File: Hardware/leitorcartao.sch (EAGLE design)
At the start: 161 parts, among them IC1 TL084, IC2 TL084, Q1 DMN3404, Q4 BC847ALT1SMD, Q5 BC847ALT1SMD, Q6 BC847ALT1SMD, Q7 BC847ALT1SMD, Q8 MMBT4403, Q9 MMBT4401, U1 SAMD20E14A-AUT, U3 TLV1117-50CDCYR, U4 MFRC52202HN1, U5 LP2985-33DBVR, X1 MIFARE, X3 ANTENA, Y1 27.12MHz

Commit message: Mais progressos em isolar todos os componentes na camada superior.
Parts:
- removed SJ?1: SOLDERBRIDGE, RFiD:SOLDERBRIDGE
- added JP1: (no value), pinhead:PINHD-2X3
- Y1: device RFiD:CRISTALSMALL(3.2X2.5MM) -> ACESSO:CRISTALSMALL(3.2X2.5MM); CUSTOMER_PN XTAL/2712MHZ/3x2 -> (none)
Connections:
- removed net N$77: R44.2, SG1.+, SJ?1.2
- net +12V: now also R44.2, SG1.+; no longer SJ?1.1
- net +3V3: no longer SJ?1.3
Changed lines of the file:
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@@
 <part name="GND42" library="supply1" deviceset="GND" device=""/>
 <part name="GND43" library="supply1" deviceset="GND" device=""/>
-<part name="Y1" library="RFiD" deviceset="CRISTAL" device="SMALL(3.2X2.5MM)" value="27.12MHz">
-<attribute name="CUSTOMER_PN" value="XTAL/2712MHZ/3x2"/>
-</part>
 <part name="C5" library="RFiD" deviceset="C-US" device="C0402" value="18p">
 <attribute name="CUSTOMER_PN" value="C/18p/16V/C04"/>
@@
 <attribute name="CUSTOMER_PN" value="R/1k/5%/04"/>
 </part>
-<part name="+3V16" library="supply1" deviceset="+3V3" device=""/>
 <part name="D5" library="RFiD" deviceset="BAT54S" device="">
 <attribute name="CUSTOMER_PN" value="D/BAT54S"/>
@@
 <part name="P+10" library="supply1" deviceset="V+" device=""/>
 <part name="P+12" library="supply1" deviceset="+12V" device=""/>
-<part name="SJ?1" library="RFiD" deviceset="SOLDERBRIDGE" device=""/>
 <part name="P+16" library="supply1" deviceset="+12V" device=""/>
 <part name="C43" library="RFiD" deviceset="C-US" device="C0402" value="0.1u"/>
@@
 <part name="C60" library="RFiD" deviceset="C-US" device="C0402" value="0.1u"/>
 <part name="GND30" library="supply1" deviceset="GND" device=""/>
+<part name="JP1" library="pinhead" deviceset="PINHD-2X3" device=""/>
+<part name="Y1" library="ACESSO" deviceset="CRISTAL" device="SMALL(3.2X2.5MM)" value="27.12MHz"/>
 </parts>
 <sheets>
@@
 <instance part="X3" gate="-1" x="45.72" y="134.62"/>
 <instance part="X3" gate="-2" x="45.72" y="132.08"/>
+<instance part="JP1" gate="A" x="-17.78" y="55.88"/>
 </instances>
 <busses>
@@
 <instance part="GND42" gate="1" x="200.66" y="152.4"/>
 <instance part="GND43" gate="1" x="213.36" y="152.4"/>
-<instance part="Y1" gate="G$1" x="43.18" y="137.16" smashed="yes" rot="R90">
-<attribute name="NAME" x="45.72" y="140.716" size="1.778" layer="95"/>
-<attribute name="VALUE" x="45.212" y="131.318" size="1.778" layer="96"/>
-<attribute name="CUSTOMER_PN" x="43.18" y="137.16" size="1.778" layer="96" display="off"/>
-</instance>
 <instance part="C5" gate="G$1" x="38.1" y="149.86" smashed="yes" rot="R270">
 <attribute name="NAME" x="33.528" y="153.035" size="1.778" layer="95"/>
@@
 <instance part="X1" gate="-1" x="243.84" y="66.04"/>
 <instance part="X1" gate="-2" x="243.84" y="63.5"/>
+<instance part="Y1" gate="G$1" x="43.18" y="137.16" smashed="yes" rot="R90">
+<attribute name="NAME" x="41.656" y="141.732" size="1.778" layer="95" rot="R180"/>
+<attribute name="VALUE" x="56.388" y="133.604" size="1.778" layer="96" rot="R180"/>
+</instance>
 </instances>
 <busses>
@@
 </segment>
 <segment>
-<pinref part="Y1" gate="G$1" pin="GND@2"/>
 <pinref part="GND14" gate="1" pin="GND"/>
 <wire x1="38.1" y1="137.16" x2="30.48" y2="137.16" width="0.1524" layer="91"/>
@@
 <wire x1="33.02" y1="124.46" x2="30.48" y2="124.46" width="0.1524" layer="91"/>
 <wire x1="30.48" y1="124.46" x2="30.48" y2="137.16" width="0.1524" layer="91"/>
+<pinref part="Y1" gate="G$1" pin="GND@2"/>
 </segment>
 <segment>
 <pinref part="GND13" gate="1" pin="GND"/>
-<pinref part="Y1" gate="G$1" pin="GND@1"/>
 <wire x1="50.8" y1="137.16" x2="48.26" y2="137.16" width="0.1524" layer="91"/>
+<pinref part="Y1" gate="G$1" pin="GND@1"/>
 </segment>
 <segment>
@@
 <wire x1="66.04" y1="139.7" x2="60.96" y2="139.7" width="0.1524" layer="91"/>
 <wire x1="60.96" y1="139.7" x2="60.96" y2="144.78" width="0.1524" layer="91"/>
-<pinref part="Y1" gate="G$1" pin="2"/>
 <wire x1="60.96" y1="144.78" x2="43.18" y2="144.78" width="0.1524" layer="91"/>
 <wire x1="43.18" y1="144.78" x2="43.18" y2="139.7" width="0.1524" layer="91"/>
@@
 <pinref part="C5" gate="G$1" pin="1"/>
 <wire x1="43.18" y1="149.86" x2="40.64" y2="149.86" width="0.1524" layer="91"/>
+<pinref part="Y1" gate="G$1" pin="2"/>
 </segment>
 </net>
@@
 <wire x1="66.04" y1="134.62" x2="60.96" y2="134.62" width="0.1524" layer="91"/>
 <wire x1="60.96" y1="134.62" x2="60.96" y2="129.54" width="0.1524" layer="91"/>
-<pinref part="Y1" gate="G$1" pin="1"/>
 <wire x1="60.96" y1="129.54" x2="43.18" y2="129.54" width="0.1524" layer="91"/>
 <wire x1="43.18" y1="129.54" x2="43.18" y2="134.62" width="0.1524" layer="91"/>
@@
 <wire x1="43.18" y1="124.46" x2="43.18" y2="129.54" width="0.1524" layer="91"/>
 <junction x="43.18" y="129.54"/>
+<pinref part="Y1" gate="G$1" pin="1"/>
 </segment>
 </net>
@@
 <attribute name="CUSTOMER_PN" x="35.56" y="139.7" size="1.778" layer="96" display="off"/>
 </instance>
-<instance part="+3V16" gate="G$1" x="25.4" y="162.56"/>
 <instance part="D5" gate="G$1" x="208.28" y="157.48" rot="R180">
 <attribute name="CUSTOMER_PN" x="208.28" y="157.48" size="1.778" layer="96" display="off"/>
@@
 <instance part="+3V18" gate="G$1" x="198.12" y="162.56"/>
 <instance part="+3V19" gate="G$1" x="198.12" y="132.08"/>
-<instance part="SJ?1" gate="G$1" x="35.56" y="154.94" rot="R180"/>
-<instance part="P+16" gate="1" x="48.26" y="162.56"/>
+<instance part="P+16" gate="1" x="35.56" y="154.94"/>
 <instance part="LED2" gate="G$1" x="109.22" y="124.46"/>
 <instance part="GND19" gate="1" x="106.68" y="114.3"/>
@@
 <wire x1="198.12" y1="127" x2="198.12" y2="129.54" width="0.1524" layer="91"/>
 </segment>
-<segment>
-<pinref part="+3V16" gate="G$1" pin="+3V3"/>
-<pinref part="SJ?1" gate="G$1" pin="3"/>
-<wire x1="25.4" y1="160.02" x2="25.4" y2="154.94" width="0.1524" layer="91"/>
-<wire x1="25.4" y1="154.94" x2="30.48" y2="154.94" width="0.1524" layer="91"/>
-</segment>
 </net>
 <net name="N$54" class="0">
@@
 </segment>
 </net>
-<net name="+12V" class="0">
-<segment>
-<pinref part="SJ?1" gate="G$1" pin="1"/>
-<pinref part="P+16" gate="1" pin="+12V"/>
-<wire x1="40.64" y1="154.94" x2="48.26" y2="154.94" width="0.1524" layer="91"/>
-<wire x1="48.26" y1="154.94" x2="48.26" y2="160.02" width="0.1524" layer="91"/>
-</segment>
-</net>
 <net name="N$18" class="0">
 <segment>
@@
 </segment>
 </net>
-<net name="N$77" class="0">
-<segment>
-<pinref part="R44" gate="G$1" pin="2"/>
-<wire x1="35.56" y1="144.78" x2="35.56" y2="147.32" width="0.1524" layer="91"/>
-<pinref part="SG1" gate="1" pin="+"/>
-<wire x1="45.72" y1="144.78" x2="45.72" y2="147.32" width="0.1524" layer="91"/>
-<wire x1="45.72" y1="147.32" x2="35.56" y2="147.32" width="0.1524" layer="91"/>
-<pinref part="SJ?1" gate="G$1" pin="2"/>
-<wire x1="35.56" y1="147.32" x2="35.56" y2="152.4" width="0.1524" layer="91"/>
-<junction x="35.56" y="147.32"/>
-</segment>
-</net>
 <net name="N$52" class="0">
 <segment>
@@
 </segment>
 </net>
+<net name="+12V" class="0">
+<segment>
+<pinref part="R44" gate="G$1" pin="2"/>
+<wire x1="35.56" y1="144.78" x2="35.56" y2="147.32" width="0.1524" layer="91"/>
+<pinref part="SG1" gate="1" pin="+"/>
+<wire x1="45.72" y1="144.78" x2="45.72" y2="147.32" width="0.1524" layer="91"/>
+<wire x1="45.72" y1="147.32" x2="35.56" y2="147.32" width="0.1524" layer="91"/>
+<wire x1="35.56" y1="147.32" x2="35.56" y2="152.4" width="0.1524" layer="91"/>
+<junction x="35.56" y="147.32"/>
+<pinref part="P+16" gate="1" pin="+12V"/>
+</segment>
+</net>

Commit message: Última versão do posicionamento.
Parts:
- removed JP1: (no value), pinhead:PINHD-2X3
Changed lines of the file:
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@@
 <part name="C60" library="RFiD" deviceset="C-US" device="C0402" value="0.1u"/>
 <part name="GND30" library="supply1" deviceset="GND" device=""/>
-<part name="JP1" library="pinhead" deviceset="PINHD-2X3" device=""/>
 <part name="Y1" library="ACESSO" deviceset="CRISTAL" device="SMALL(3.2X2.5MM)" value="27.12MHz"/>
 </parts>
@@
 <instance part="X3" gate="-1" x="45.72" y="134.62"/>
 <instance part="X3" gate="-2" x="45.72" y="132.08"/>
-<instance part="JP1" gate="A" x="-17.78" y="55.88"/>
 </instances>
 <busses>

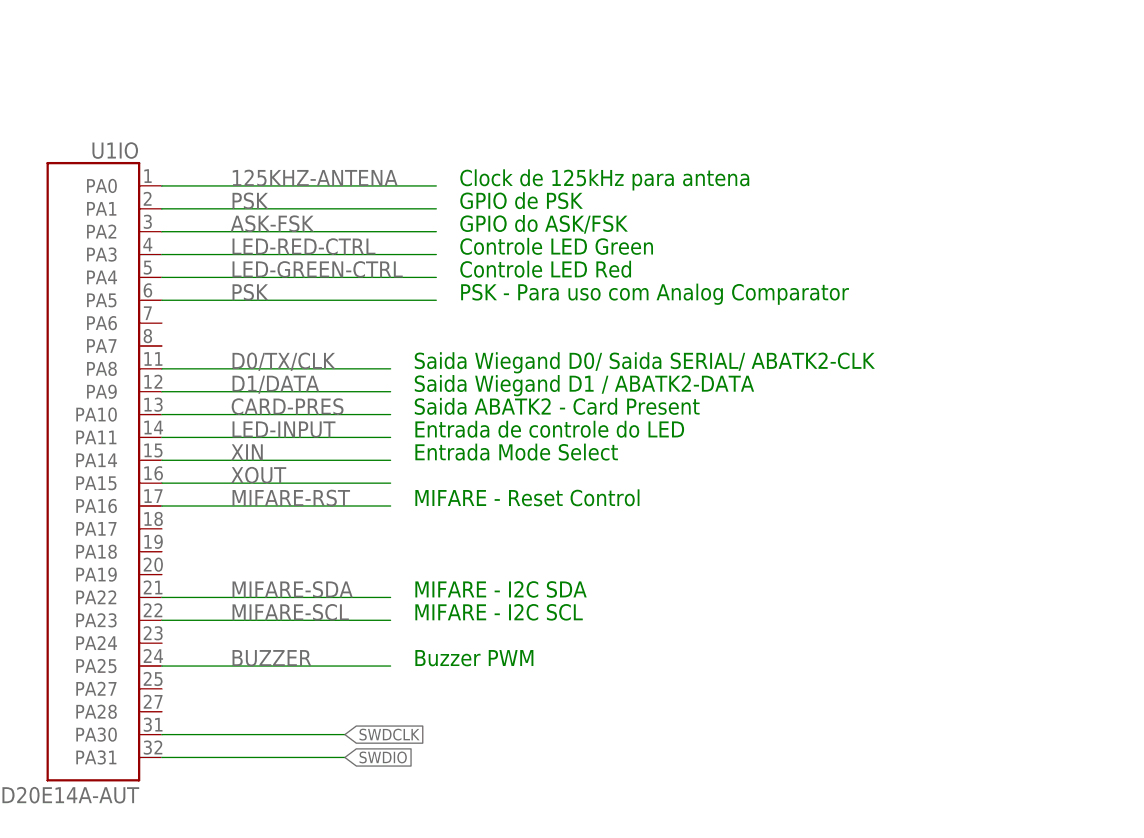
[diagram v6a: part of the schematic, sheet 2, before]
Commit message: Roteamento finalizado, polígonos criados e silks criados.
Necessita revisão.
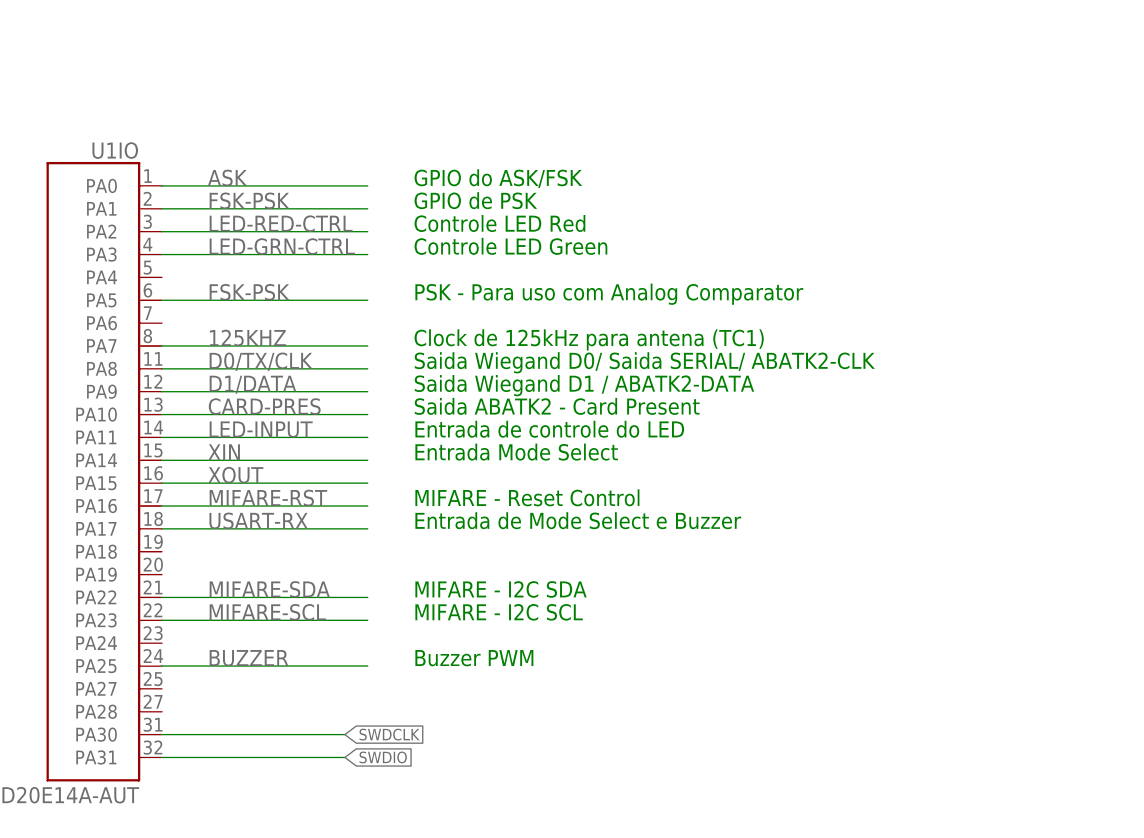
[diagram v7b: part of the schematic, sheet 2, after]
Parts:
- renumbered MODE-SEL to MODE
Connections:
- net PSK renamed FSK-PSK
- removed net 125KHZ-ANTENA: R5.1, U1IO.PA0
- removed net ASK-FSK: R45.2, R59.2, U1IO.PA2
- removed net LED-GREEN-CTRL: R41.1, U1IO.PA4
- new net 125KHZ: R5.1, U1IO.PA7
- new net ASK-OUT: C18.1, C22.2, C26.2, IC1B.OUT, R10.1, R9.1
- new net LED-GRN-CTRL: R41.1, U1IO.PA3
- net ASK: now also R45.2, R59.2, U1IO.PA0; no longer C18.1, C22.2, C26.2, IC1B.OUT, R10.1, R9.1
- net LED-RED-CTRL: now also U1IO.PA2; no longer U1IO.PA3
- net USART-RX: now also U1IO.PA17
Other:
- note added: "Clock de 125kHz para antena (TC1)"
- note added: "Entrada de Mode Select e Buzzer"
- note removed: "Clock de 125kHz para antena"
- moved on the sheet: C26
